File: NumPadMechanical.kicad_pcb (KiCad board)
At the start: 2 copper layers, 91.5 x 110.5 mm, 85 parts, among them J1 USB_C_Receptacle_USB2.0_14P, SW1 SW_SPDT, U1 STM32F103CBT6, U2 AMS1117-3.3, Y1 Crystal

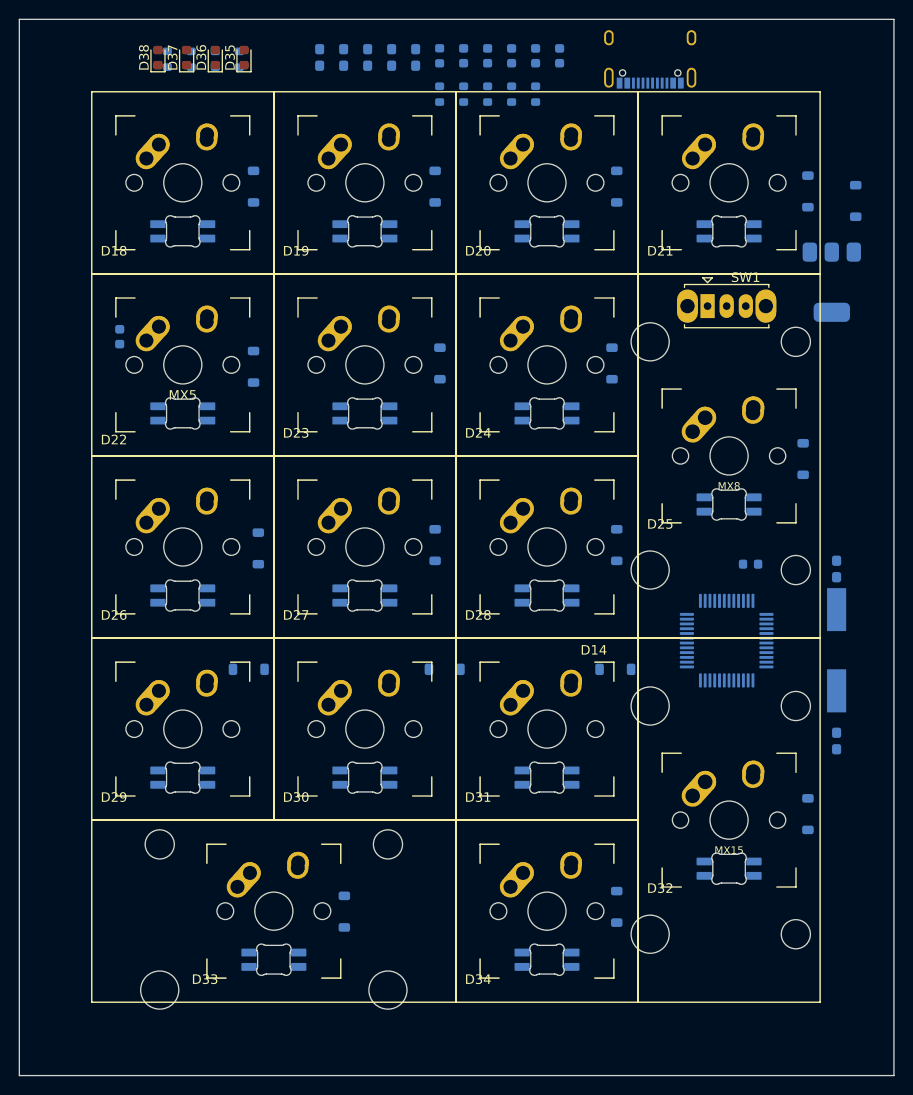
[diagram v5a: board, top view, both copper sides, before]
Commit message: Se hacen modificaciones en la pcb acomodando los dispositivos y se agrega tierra comun en ambos lados de la placa
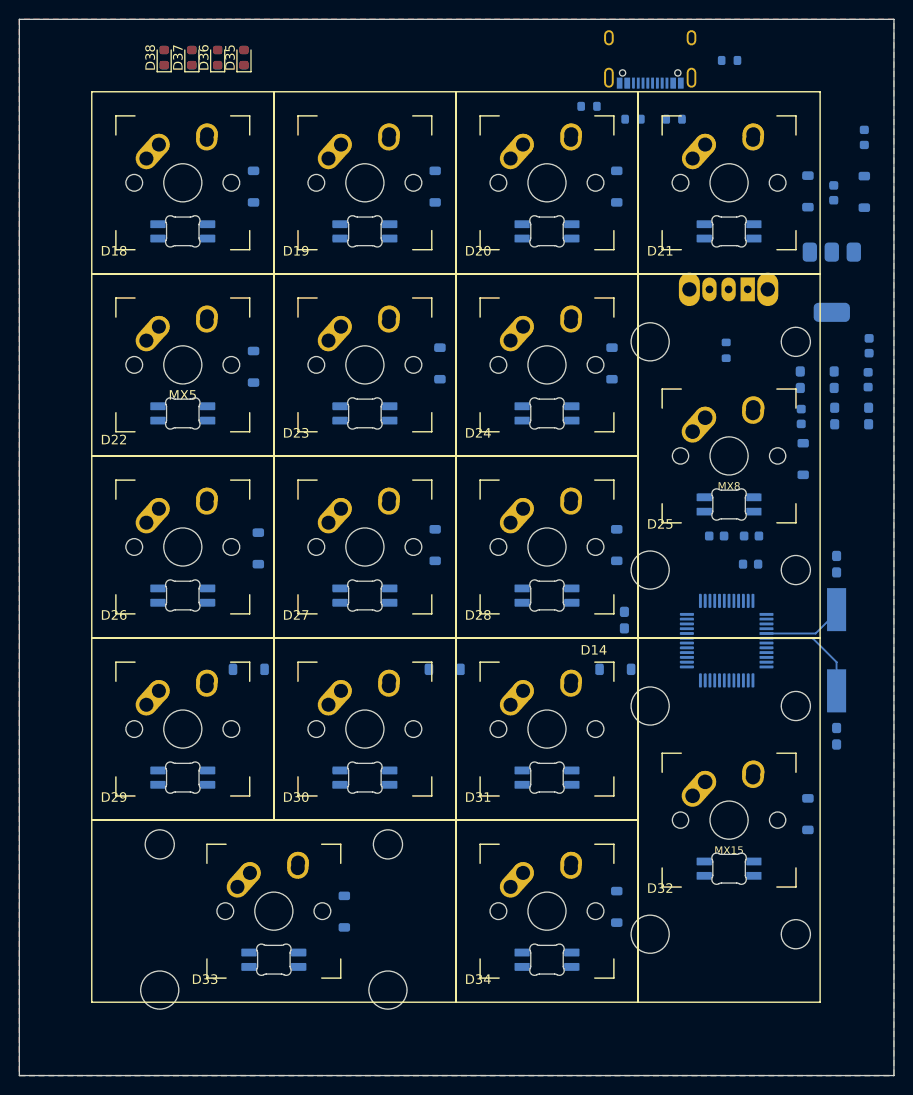
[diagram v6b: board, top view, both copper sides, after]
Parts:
- SW1: moved to B.Cu
- moved C2 71.8 mm to (102.8, 62.5), turned to -90 degrees
- moved C11 66.9 mm to (84.3, 83.8)
- moved C4 62.4 mm to (109.8, 62.5), turned to -90 degrees
- moved C6 61.4 mm to (106.2, 58.7)
- moved C3 57.7 mm to (106.3, 62.5), turned to -90 degrees
- moved C9 57.3 mm to (97.6, 75.0), turned to 0 degrees
- moved C5 56.4 mm to (102.7, 58.7)
- moved C8 54.6 mm to (94.0, 75.0), turned to 0 degrees
- moved C10 52.2 mm to (109.9, 55.1), turned to -90 degrees
- moved C7 48.6 mm to (109.8, 58.7)
- moved F1 45.2 mm to (109.4, 33.4), turned to -90 degrees
- moved R5 40.2 mm to (95.0, 55.6)
- moved C1 32.1 mm to (106.2, 39.1)
- moved R4 28.0 mm to (95.3, 25.3), turned to 0 degrees
- moved R1 14.7 mm to (89.5, 31.4), turned to 0 degrees
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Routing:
- net OSC_OUT: track 0.00 -> 11.4 mm
- net OSC_IN: track 0.00 -> 8.55 mm
- added copper zone on B.Cu, net GND
- added copper zone on F.Cu, net GND
